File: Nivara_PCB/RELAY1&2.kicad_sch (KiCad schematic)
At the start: 3 parts, among them K1 SRA-24VDC-CL, K2 SRA-24VDC-CL, U14 LK1802

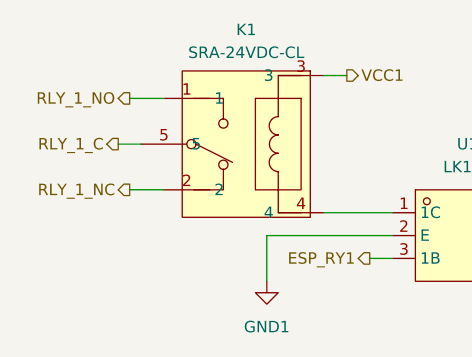
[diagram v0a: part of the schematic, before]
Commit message: Cambios en el PCB de Nivara. Ruteo de emtradas y salidas NPN y PNP.
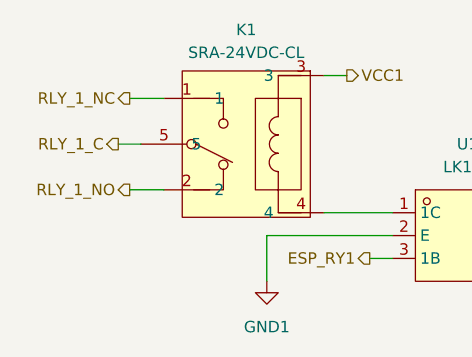
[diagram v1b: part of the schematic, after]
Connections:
- net RLY_1_NC: now also K1.1; no longer K1.2
- net RLY_1_NO: now also K1.2; no longer K1.1
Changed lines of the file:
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@@
+		)
+	)
+	(hierarchical_label "ESP_RLY2"
+		(shape output)
+		(at 133.35 71.12 0)
+		(effects
+			(font
+				(size 1.27 1.27)
+			)
+			(justify left)
+		)
+	)
+	(hierarchical_label "ESP_RY1"
+		(shape output)
+		(at 110.49 71.12 180)
+		(effects
+			(font
+				(size 1.27 1.27)
+			)
+			(justify right)
+		)
+	)
+	(hierarchical_label "RLY_2_NC"
+		(shape output)
+		(at 158.75 53.34 0)
+		(effects
+			(font
+				(size 1.27 1.27)
+			)
+			(justify left)
+		)
+	)
+	(hierarchical_label "VCC1"
+		(shape output)
+		(at 134.62 50.8 180)
+		(effects
+			(font
+				(size 1.27 1.27)
+			)
+			(justify right)
 		)
 	)
 	(hierarchical_label "RLY_1_NC"
 		(shape output)
+		(at 83.82 53.34 180)
+		(effects
+			(font
+				(size 1.27 1.27)
+			)
+			(justify right)
+		)
+	)
+	(hierarchical_label "RLY_1_C"
+		(shape output)
+		(at 82.55 58.42 180)
+		(effects
+			(font
+				(size 1.27 1.27)
+			)
+			(justify right)
+		)
+	)
+	(hierarchical_label "RLY_2_NO"
+		(shape output)
+		(at 158.75 63.5 0)
+		(effects
+			(font
+				(size 1.27 1.27)
+			)
+			(justify left)
+		)
+	)
+	(hierarchical_label "VCC1"
+		(shape output)
+		(at 133.35 68.58 0)
+		(effects
+			(font
+				(size 1.27 1.27)
+			)
+			(justify left)
+		)
+	)
+	(hierarchical_label "RLY_1_NO"
+		(shape output)
 		(at 83.82 63.5 180)
 		(effects
@@
 			)
 			(justify right)
-		)
-	)
-	(hierarchical_label "ESP_RLY2"
-		(shape output)
-		(at 133.35 71.12 0)
-		(effects
-			(font
-				(size 1.27 1.27)
-			)
-			(justify left)
-		)
-	)
-	(hierarchical_label "ESP_RY1"
-		(shape output)
-		(at 110.49 71.12 180)
-		(effects
-			(font
-				(size 1.27 1.27)
-			)
-			(justify right)
-		)
-	)
-	(hierarchical_label "RLY_2_NC"
-		(shape output)
-		(at 158.75 53.34 0)
-		(effects
-			(font
-				(size 1.27 1.27)
-			)
-			(justify left)
-		)
-	)
-	(hierarchical_label "VCC1"
-		(shape output)
-		(at 134.62 50.8 180)
-		(effects
-			(font
-				(size 1.27 1.27)
-			)
-			(justify right)
-		)
-	)
-	(hierarchical_label "RLY_1_C"
-		(shape output)
-		(at 82.55 58.42 180)
-		(effects
-			(font
-				(size 1.27 1.27)
-			)
-			(justify right)
-		)
-	)
-	(hierarchical_label "RLY_2_NO"
-		(shape output)
-		(at 158.75 63.5 0)
-		(effects
-			(font
-				(size 1.27 1.27)
-			)
-			(justify left)
-		)
-	)
-	(hierarchical_label "RLY_1_NO"
-		(shape output)
-		(at 83.82 53.34 180)
-		(effects
-			(font
-				(size 1.27 1.27)
-			)
-			(justify right)
-		)
-	)
-	(hierarchical_label "VCC1"
-		(shape output)
-		(at 133.35 68.58 0)
-		(effects
-			(font
-				(size 1.27 1.27)
-			)
-			(justify left)
 		)
 	)
@@
 		(dnp no)
 		(fields_autoplaced yes)
-		(property "Reference" "#PWR049"
+		(property "Reference" "#PWR070"
 			(at 99.06 80.01 0)
 			(effects
@@
 			(project ""
 				(path "/13184db0-a71d-4054-b13a-bbf46d2b100d/4e7fa7f2-8bf5-4f9c-874d-fa1b4fd76f92/28adab20-3df9-4bd0-b792-64ff7180ad7f"
-					(reference "#PWR049")
+					(reference "#PWR070")
 					(unit 1)
 				)

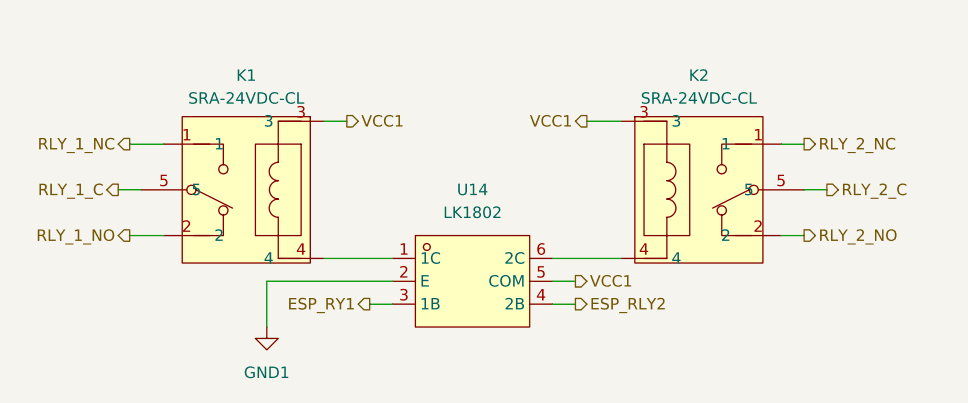
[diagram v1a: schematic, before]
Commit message: Cambios realizados en el PCB y el esquema de Nivara_PCB.
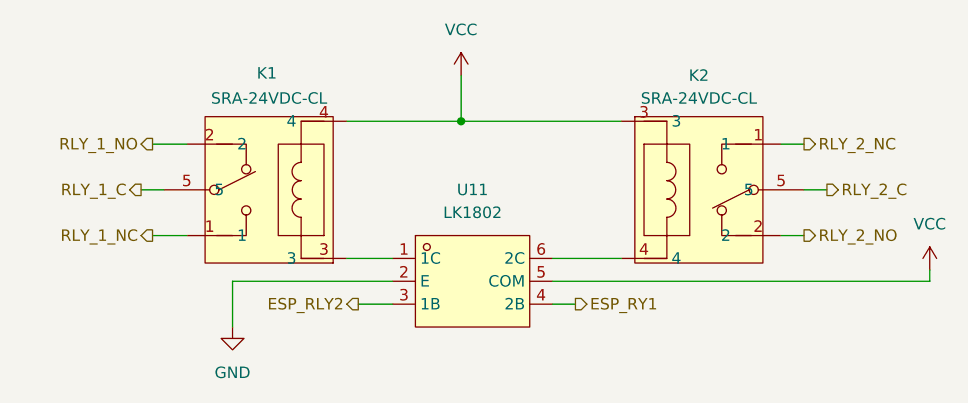
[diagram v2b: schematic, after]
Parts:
- renumbered U14 to U11
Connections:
- net ESP_RLY2: now also U11.3 (1B); no longer U11.4 (2B)
- net ESP_RY1: now also U11.4 (2B); no longer U11.3 (1B)
- net at U11.1 (1C): now also K1.3; no longer K1.4
- net GND1 renamed GND
- net VCC1 renamed VCC
- net VCC: now also K1.4; no longer K1.3
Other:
- moved on the sheet: K1

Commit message: cAMBIOS EN EL PCB Y ESQUEMA.
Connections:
- net RLY_1_NC: now also K1.2; no longer K1.1
- net RLY_1_NO: now also K1.1; no longer K1.2
- net RLY_2_NC: now also K2.2; no longer K2.1
- net RLY_2_NO: now also K2.1; no longer K2.2
- net VCC: now also K1.3, K2.4; no longer K1.4, K2.3
- net at U11.6 (2C): now also K2.3; no longer K2.4
- net at U11.1 (1C): now also K1.4; no longer K1.3
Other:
- moved on the sheet: K1
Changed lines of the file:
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@@
 		(lib_id "EasyEDA:SRA-24VDC-CL")
 		(at 148.59 58.42 0)
-		(unit 1)
-		(exclude_from_sim no)
-		(in_bom yes)
-		(on_board yes)
-		(dnp no)
-		(fields_autoplaced yes)
+		(mirror x)
+		(unit 1)
+		(exclude_from_sim no)
+		(in_bom yes)
+		(on_board yes)
+		(dnp no)
 		(property "Reference" "K2"
-			(at 147.065 45.72 0)
+			(at 147.065 71.12 0)
 			(effects
 				(font
@@
 		)
 		(property "Value" "SRA-24VDC-CL"
-			(at 147.065 48.26 0)
+			(at 147.065 68.58 0)
 			(effects
 				(font
@@
 		)
 		(property "Footprint" "EasyEDA:RELAY-TH_SRA-X-CX"
-			(at 148.59 73.66 0)
+			(at 148.59 43.18 0)
 			(effects
 				(font
@@
 		)
 		(property "Datasheet" "https://lcsc.com/product-detail/Relays_SRA-24VDC-CL_C127865.html"
-			(at 148.59 76.2 0)
+			(at 148.59 40.64 0)
 			(effects
 				(font
@@
 		)
 		(property "LCSC Part" "C127865"
-			(at 148.59 78.74 0)
+			(at 148.59 38.1 0)
 			(effects
 				(font
@@
 	(symbol
 		(lib_id "EasyEDA:SRA-24VDC-CL")
-		(at 97.79 58.42 180)
+		(at 97.79 58.42 0)
+		(mirror y)
 		(unit 1)
 		(exclude_from_sim no)
@@
 		(dnp no)
 		(property "Reference" "K1"
-			(at 99.06 45.466 0)
+			(at 99.06 71.374 0)
 			(effects
 				(font
@@
 		)
 		(property "Value" "SRA-24VDC-CL"
-			(at 99.314 48.26 0)
+			(at 99.314 68.58 0)
 			(effects
 				(font
@@
 		)
 		(property "Footprint" "EasyEDA:RELAY-TH_SRA-X-CX"
-			(at 97.79 43.18 0)
+			(at 97.79 73.66 0)
 			(effects
 				(font
@@
 		)
 		(property "Datasheet" "https://lcsc.com/product-detail/Relays_SRA-24VDC-CL_C127865.html"
-			(at 97.79 40.64 0)
+			(at 97.79 76.2 0)
 			(effects
 				(font
@@
 		)
 		(property "LCSC Part" "C127865"
-			(at 97.79 38.1 0)
-			(effects
-				(font
+			(at 97.79 78.74 0)
+			(effects
+				(font
